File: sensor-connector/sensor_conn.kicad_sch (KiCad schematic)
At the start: 11 parts, among them J1 SPS30 RS232, J2 SPS30 TTL, U1 MAX232A

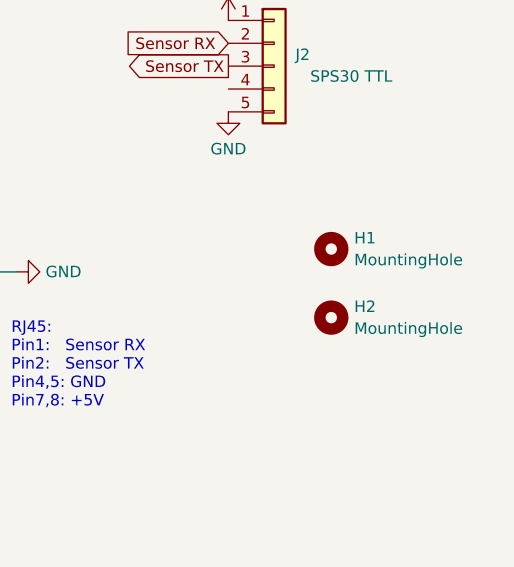
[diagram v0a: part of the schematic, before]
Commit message: changed mounting holes
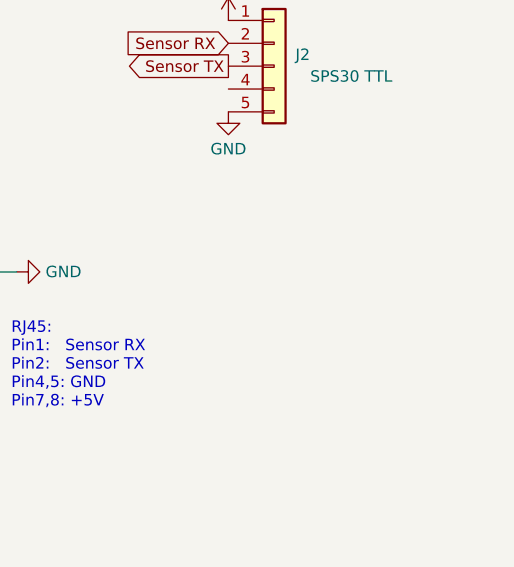
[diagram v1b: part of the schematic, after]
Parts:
- removed H1, H2: MountingHole, MountingHole:MountingHole_4.3mm_M4, symbol Mechanical:MountingHole
